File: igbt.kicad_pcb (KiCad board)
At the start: 2 copper layers, 38 parts, among them J1 Conn_01x08_Female, J2 Sense_DC, J3 Sense_AC, Q1 IRG4PF50W, Q2 IRG4PF50W, Q3 IRG4PF50W, Q4 IRG4PF50W, Q5 IRG4PF50W, Q6 IRG4PF50W, U1 ACS758xCB-050B-PFF, U2 ACS758xCB-050B-PFF

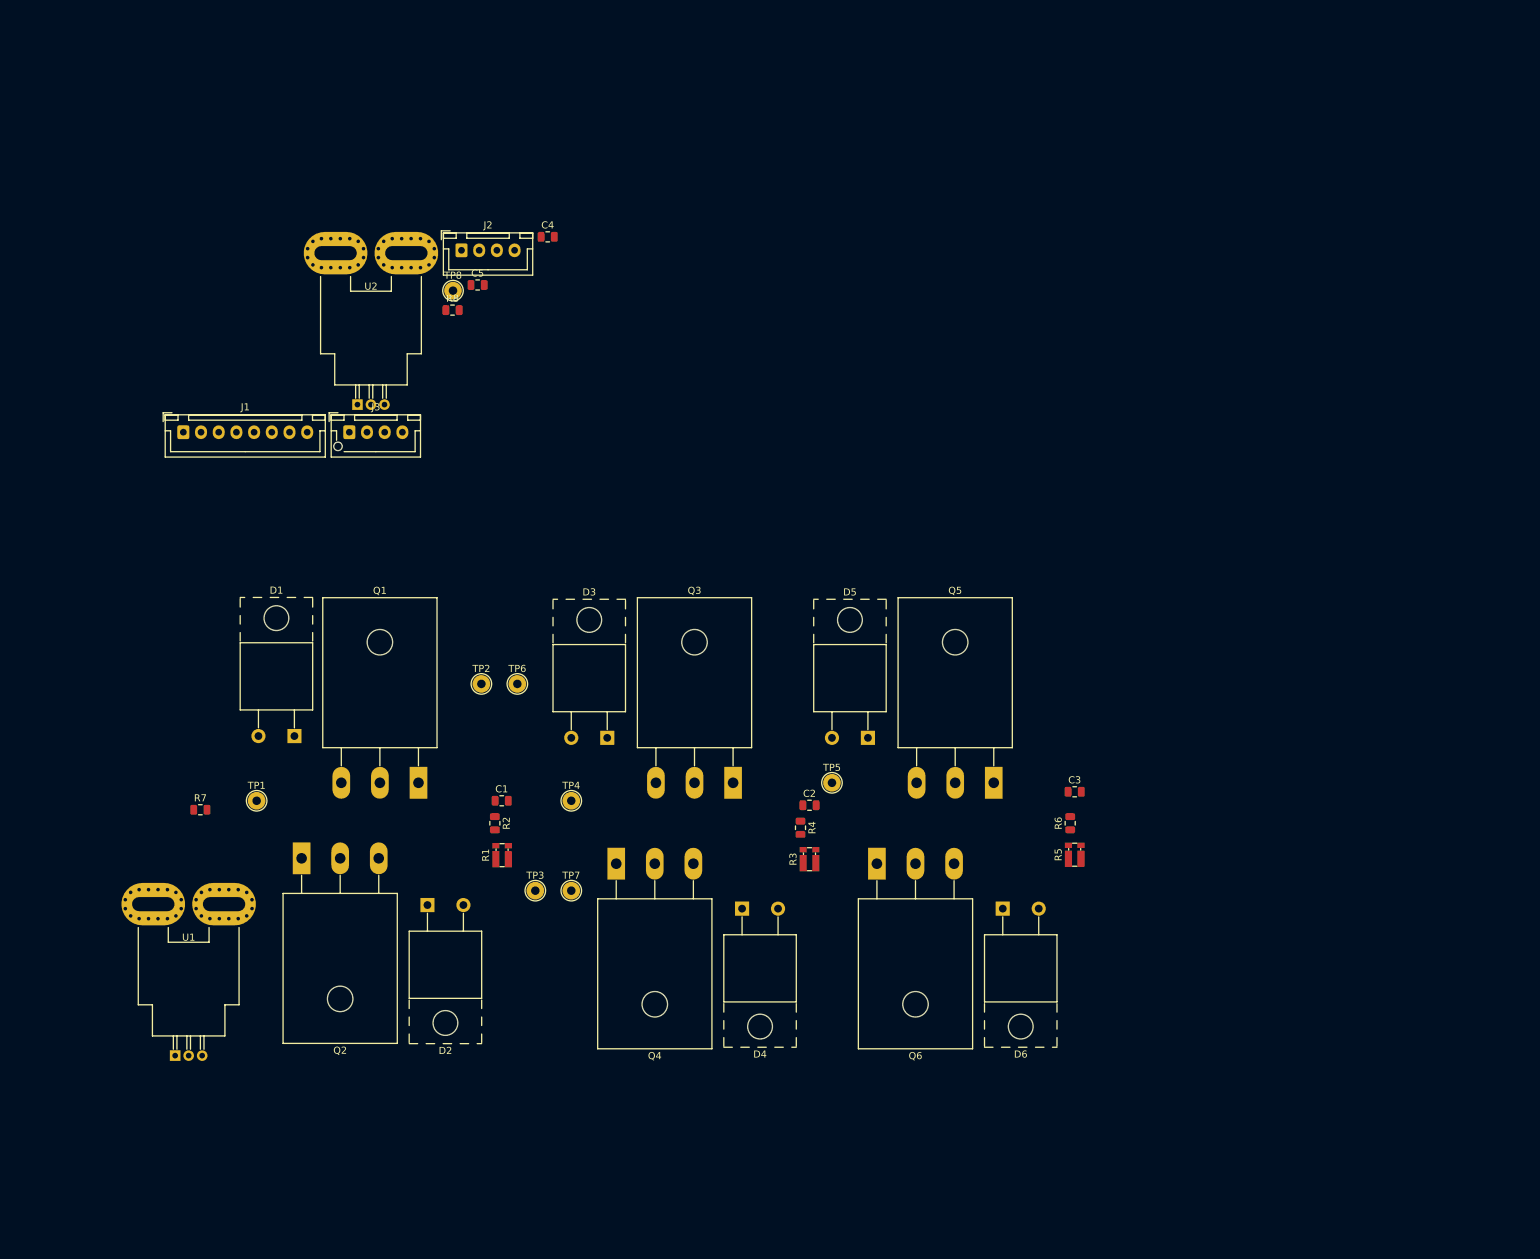
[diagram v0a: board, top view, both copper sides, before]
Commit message: shunt resistors removed
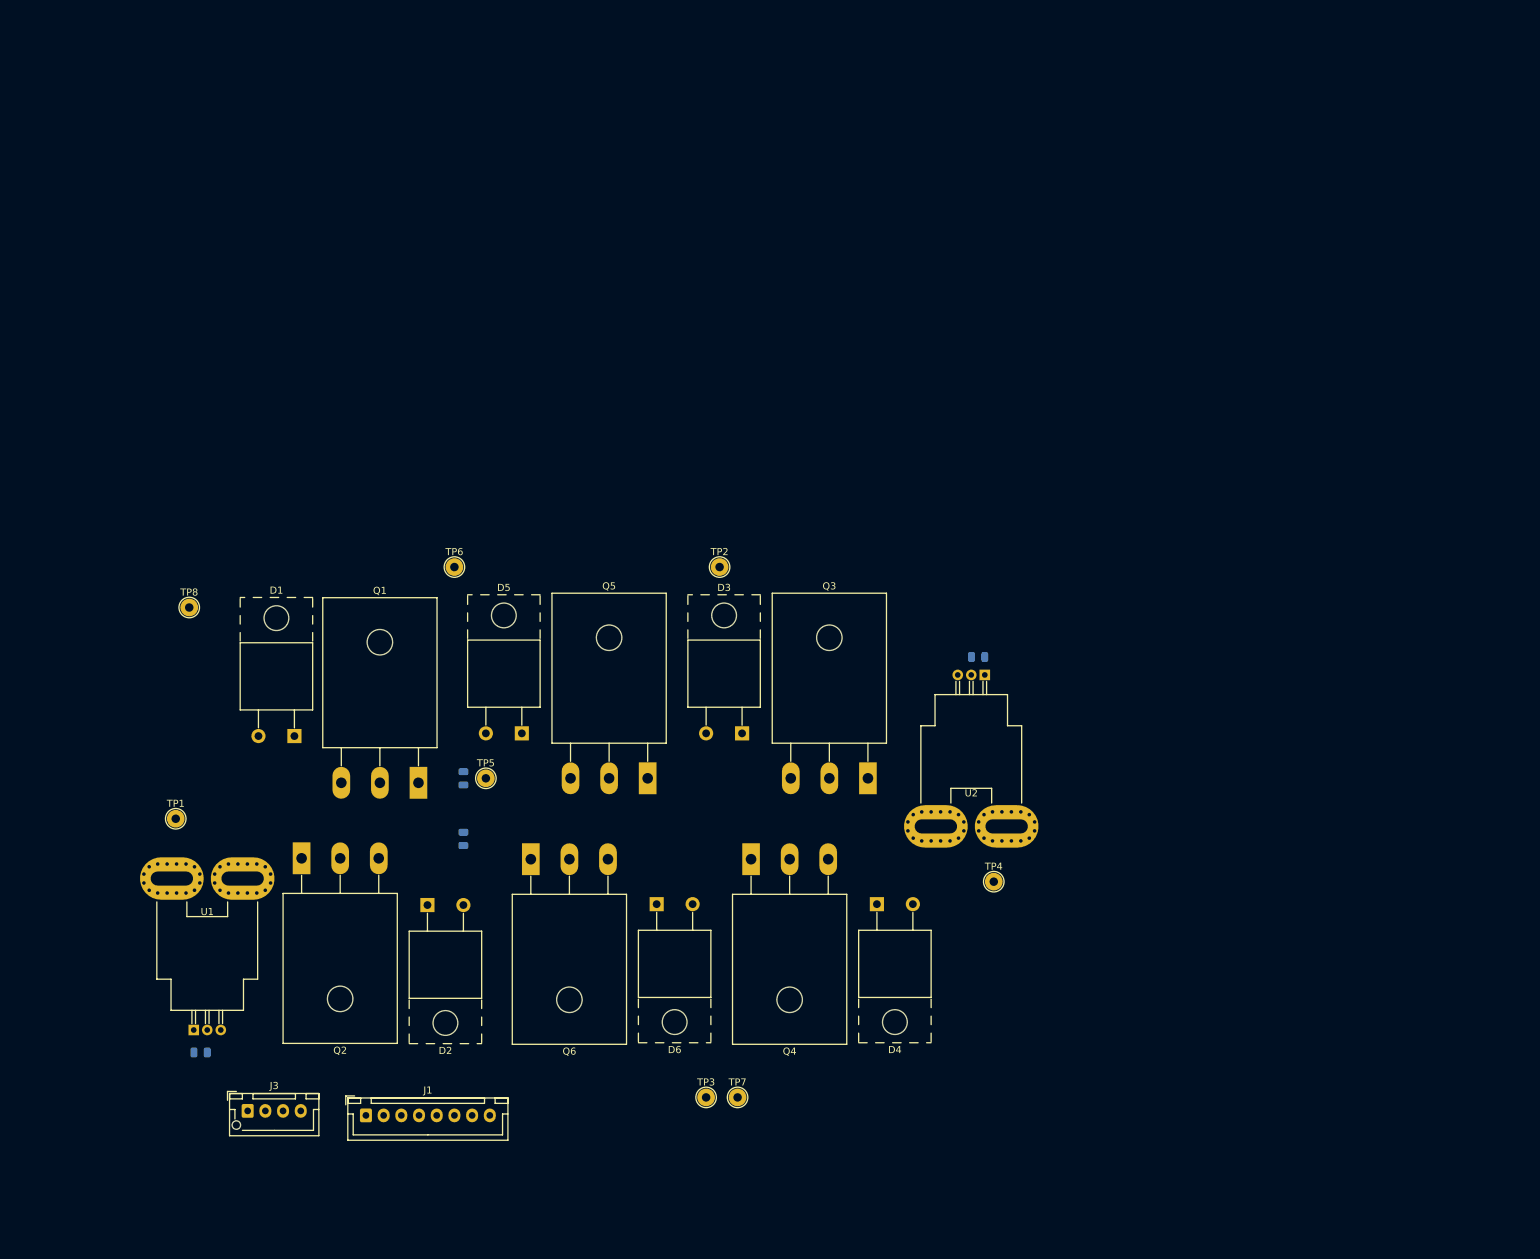
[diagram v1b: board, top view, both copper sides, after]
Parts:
- removed C1, C2, C3: 1n, Capacitor_SMD:C_0805_2012Metric
- removed J2: Sense_DC, Connector_JST:JST_XH_B04B-XH-A_1x04_P2.50mm_Vertical
- removed R1, R3, R5: R_Shunt, Resistor_SMD:R_Shunt_Vishay_WSKW0612
- removed R2, R4, R6: 1k, Resistor_SMD:R_0805_2012Metric
- C4, C5, R7, R8: moved to B.Cu
- moved C4 125.2 mm to (59.4, 165.1)
- moved J1 99.9 mm to (82.8, 174.0)
- moved J3 97.0 mm to (66.0, 173.4)
- moved U2 96.5 mm to (170.2, 111.8), turned to 180 degrees
- moved C5 88.1 mm to (169.2, 109.2)
- moved R8 74.7 mm to (96.5, 134.9), turned to 270 degrees
- moved TP4 60.8 mm to (171.4, 141.0)
- moved TP8 58.2 mm to (57.8, 102.2)
- moved TP5 48.9 mm to (99.7, 126.4)
- moved D6 48.9 mm to (123.8, 144.1)
- moved Q6 48.9 mm to (106.0, 137.8)
- moved D5 48.9 mm to (104.8, 120.0)
- moved Q5 48.9 mm to (122.6, 126.4)
- moved TP3 37.9 mm to (130.8, 171.4)
- moved TP2 37.5 mm to (132.7, 96.5)
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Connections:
- D4 pad 2: Net-(D4-Pad2) -> Net-(D2-Pad2)
- D6 pad 2: Net-(D6-Pad2) -> Net-(D2-Pad2)
- J1 pad 8: Net-(J1-Pad8) -> Net-(D2-Pad2)
- Q4 pad 3: Net-(D4-Pad2) -> Net-(D2-Pad2)
- Q6 pad 3: Net-(D6-Pad2) -> Net-(D2-Pad2)
- R8 pad 1: Net-(J1-Pad8) -> Net-(D2-Pad2)
- TP3 pad 1: Net-(J1-Pad8) -> Net-(D2-Pad2)
- TP7 pad 1: Net-(J1-Pad8) -> Net-(D2-Pad2)

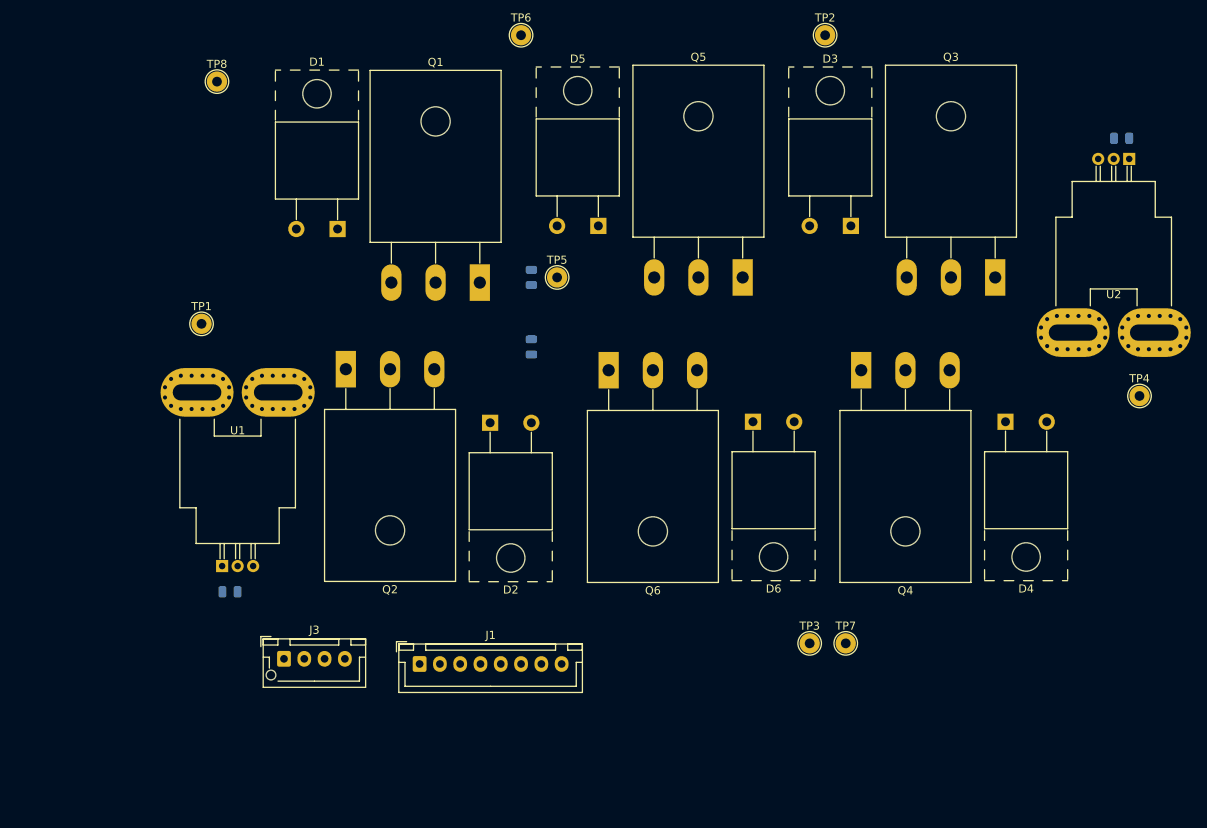
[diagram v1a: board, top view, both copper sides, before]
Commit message: separate connectors for ac current sensing
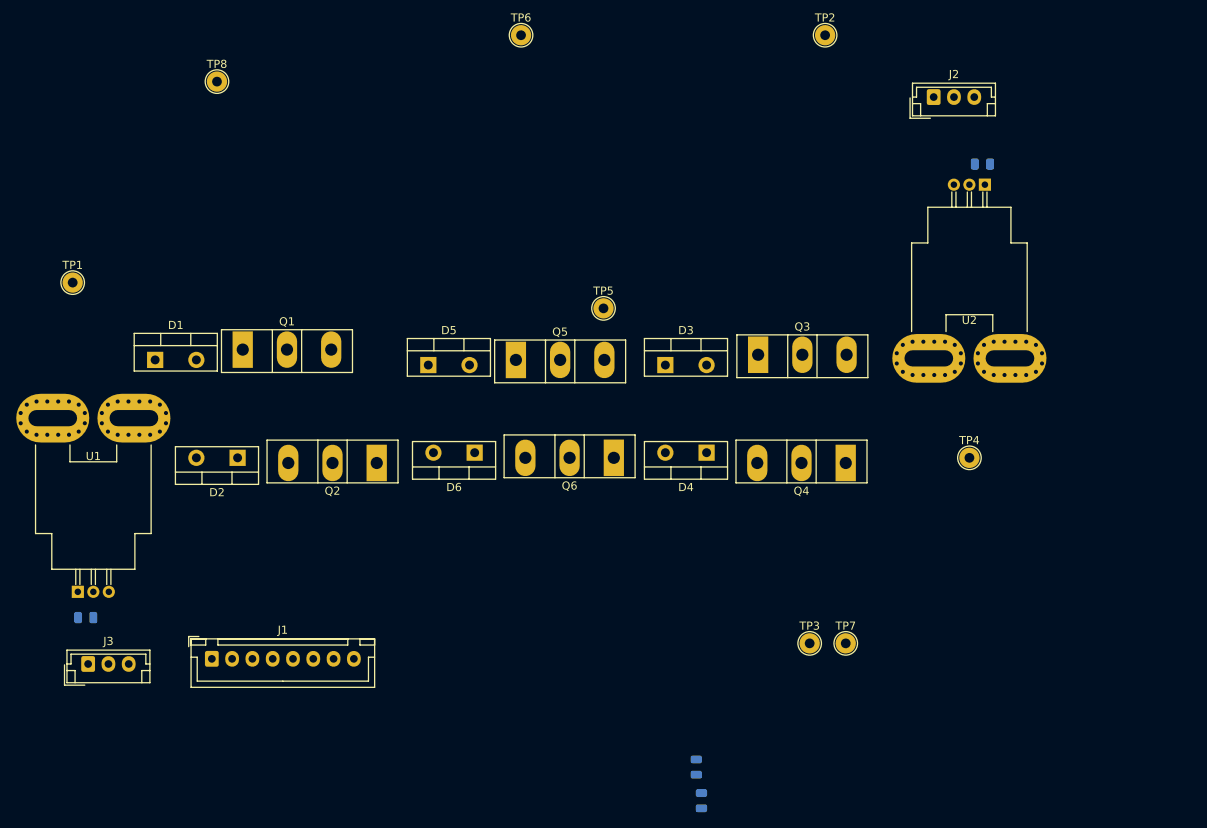
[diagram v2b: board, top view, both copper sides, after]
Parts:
- added J2: Sense_AC, Connector_JST:JST_EH_B03B-EH-A_1x03_P2.50mm_Vertical, F.Cu at (146.1, 104.1)
- D1, D2, D3, D4, D5, D6: footprint Package_TO_SOT_THT:TO-220-2_Horizontal_TabUp -> Package_TO_SOT_THT:TO-220-2_Vertical
- J1: value Conn_01x08_Female -> PWM
- J3: footprint Connector_JST:JST_XH_B04B-XH-AM_1x04_P2.50mm_Vertical -> Connector_JST:JST_EH_B03B-EH-A_1x03_P2.50mm_Vertical
- Q1, Q2, Q3, Q4, Q5, Q6: footprint Package_TO_SOT_THT:TO-247-3_Horizontal_TabUp -> Package_TO_SOT_THT:TO-247-3_Vertical
- moved R7 63.7 mm to (116.8, 186.7), turned to 90 degrees
- moved R8 59.7 mm to (117.5, 190.8), turned to 90 degrees
- moved D4 37.0 mm to (118.1, 148.0), turned to 180 degrees
- moved D6 34.5 mm to (89.5, 148.0), turned to 180 degrees
- moved D2 31.4 mm to (60.3, 148.6), turned to 180 degrees
- moved Q3 30.7 mm to (124.5, 135.9), turned to 0 degrees
- moved Q1 30.4 mm to (61.0, 135.3), turned to 0 degrees
- moved Q5 29.7 mm to (94.6, 136.5), turned to 0 degrees
- moved D3 28.6 mm to (113.0, 137.2), turned to 0 degrees
- moved D1 27.7 mm to (50.2, 136.5), turned to 0 degrees
- moved D5 27.1 mm to (83.8, 137.2), turned to 0 degrees
- moved J1 25.6 mm to (57.1, 173.4)
- moved J3 24.1 mm to (41.9, 174.0)
- moved TP4 22.3 mm to (150.5, 148.6)
- moved C4 18.1 mm to (41.6, 168.3)
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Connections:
- J3 pad 3: Net-(J3-Pad3) -> Net-(C4-Pad1)
- U1 pad 3: Net-(J3-Pad3) -> Net-(J3-Pad2)
- U2 pad 3: Net-(J3-Pad2) -> Net-(J2-Pad2)

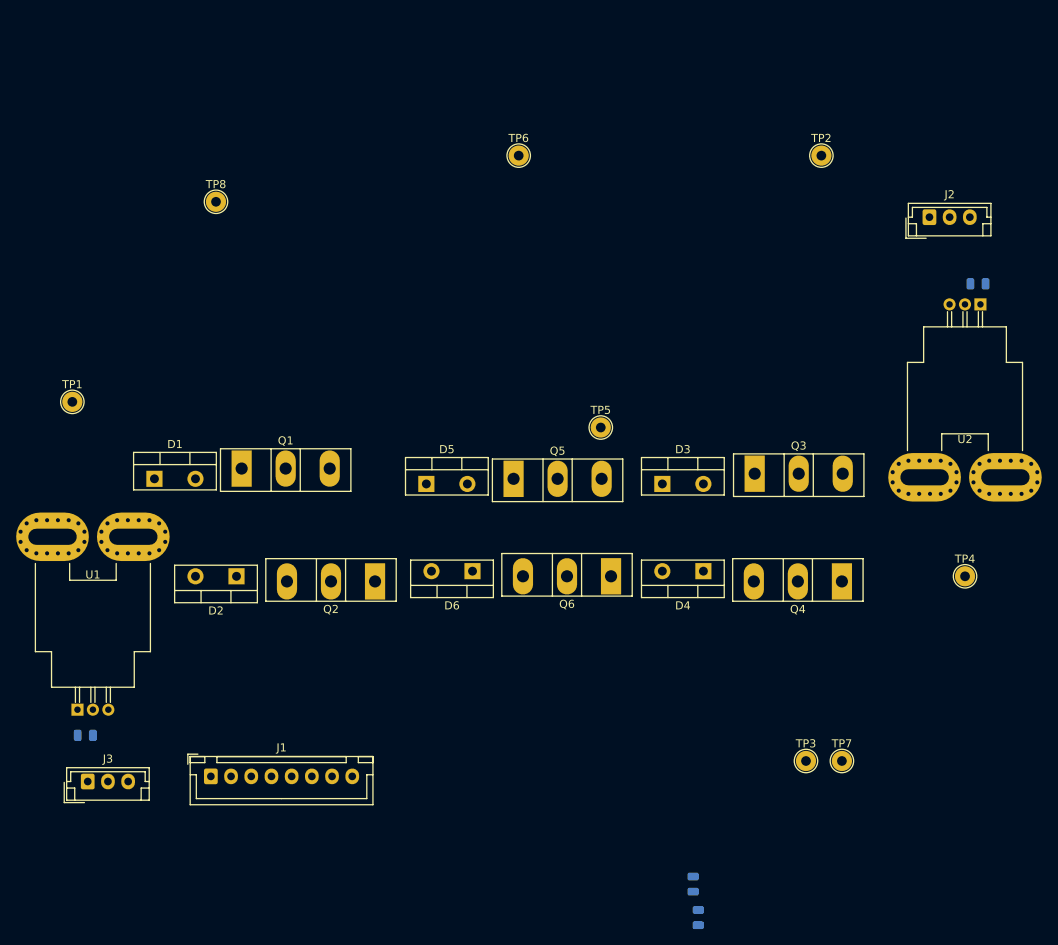
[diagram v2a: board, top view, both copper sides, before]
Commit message: igbts in U-shape
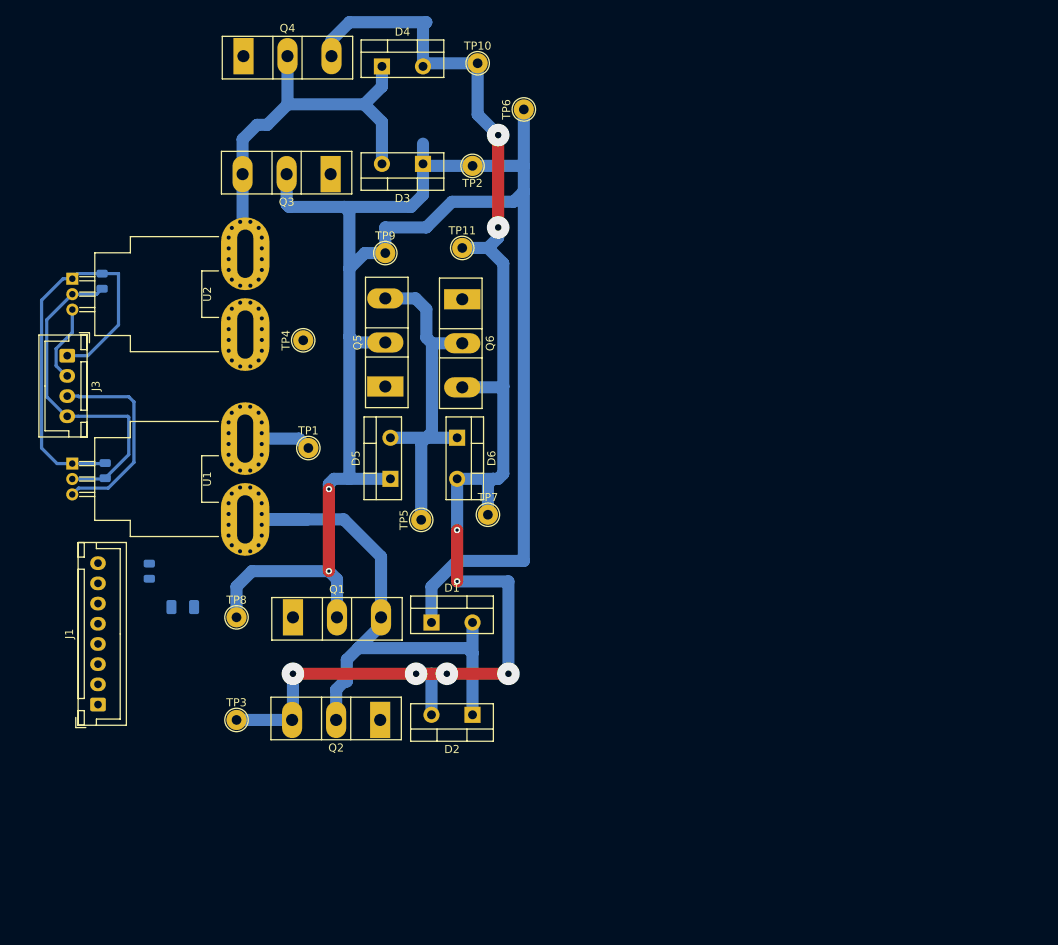
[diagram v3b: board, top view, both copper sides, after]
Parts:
- removed J2: Sense_AC, Connector_JST:JST_EH_B03B-EH-A_1x03_P2.50mm_Vertical
- added TP10: DC_CapB_N, TestPoint:TestPoint_THTPad_D2.5mm_Drill1.2mm, F.Cu at (90.2, 85.1)
- added TP11: DC_CapC_N, TestPoint:TestPoint_THTPad_D2.5mm_Drill1.2mm, F.Cu at (88.3, 108.0)
- added TP9: DC_CapC_P, TestPoint:TestPoint_THTPad_D2.5mm_Drill1.2mm, F.Cu at (78.7, 108.6)
- J3: footprint Connector_JST:JST_EH_B03B-EH-A_1x03_P2.50mm_Vertical -> Connector_JST:JST_XH_B04B-XH-A_1x04_P2.50mm_Vertical
- R7: footprint Resistor_SMD:R_0805_2012Metric -> Resistor_SMD:R_1206_3216Metric
- TP2: value DC_CapP -> DC_CapB_P
- TP3: value DC_CapN -> DC_CapA_N
- TP8: value DC_BUS -> DC_CapA_P
- moved U2 112.4 mm to (40.0, 111.8), turned to 270 degrees
- moved C5 108.4 mm to (43.7, 112.1), turned to 90 degrees
- moved Q4 98.6 mm to (61.2, 84.2), turned to 0 degrees
- moved TP4 87.0 mm to (68.6, 119.4), turned to 90 degrees
- moved R8 80.3 mm to (49.5, 148.0), turned to 270 degrees
- moved D4 74.1 mm to (78.3, 85.5), turned to 0 degrees
- moved R7 71.9 mm to (53.7, 152.4), turned to 0 degrees
- moved TP3 70.7 mm to (60.3, 166.4)
- moved Q3 64.3 mm to (72.0, 98.8), turned to 180 degrees
- moved TP7 53.4 mm to (91.4, 141.0)
- moved J3 52.8 mm to (39.4, 121.3), turned to 270 degrees
- moved TP8 51.5 mm to (60.3, 153.7)
- moved D3 49.5 mm to (83.4, 97.5), turned to 180 degrees
- moved TP2 43.2 mm to (89.5, 97.8), turned to 180 degrees
- moved Q6 38.9 mm to (88.3, 114.3), turned to 270 degrees
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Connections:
- J3 pad 1: GND -> Net-(C4-Pad1)
- J3 pad 3: Net-(C4-Pad1) -> Net-(J3-Pad3)
- U1 pad 3: Net-(J3-Pad2) -> Net-(J3-Pad3)
- U2 pad 3: Net-(J2-Pad2) -> Net-(J3-Pad2)
- U2 pad 4: Net-(D3-Pad2) -> Net-(TP4-Pad1)
- U2 pad 5: Net-(TP4-Pad1) -> Net-(D3-Pad2)
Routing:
- net Net-(D1-Pad1): track 0.00 -> 220.2 mm, vias 0 -> 2
- net Net-(D2-Pad2): track 0.00 -> 178.0 mm, vias 0 -> 8
- net Net-(D1-Pad2): track 0.00 -> 75.0 mm
- net Net-(C4-Pad1): track 0.00 -> 52.2 mm
- net Net-(D3-Pad2): track 0.00 -> 51.0 mm
- net Net-(D5-Pad2): track 0.00 -> 44.6 mm
- net GND: track 0.00 -> 42.1 mm
- net Net-(J3-Pad3): track 0.00 -> 25.3 mm
- net Net-(J3-Pad2): track 0.00 -> 9.68 mm
- net Net-(TP1-Pad1): track 0.00 -> 8.30 mm
